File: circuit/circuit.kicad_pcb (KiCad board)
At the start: 2 copper layers, 14 parts, among them J1 POWER, J2 BLUETOOTH, J3 BUZZER, SW1 SW_PUSH_6mm, U1 ADXL359

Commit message: pcb v2.1
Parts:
- added R1: R, Resistor_SMD:R_1206_3216Metric_Pad1.30x1.75mm_HandSolder, B.Cu at (126.4, 38.3)
- added SW2: SW_DPDT_x2, Connector_PinSocket_2.00mm:PinSocket_1x03_P2.00mm_Vertical, F.Cu at (134.2, 42.2)
- C1, C2, C3, C4, C5, C6, C7, C8, U1: moved to B.Cu
- J1: footprint Connector_PinSocket_1.00mm:PinSocket_1x02_P1.00mm_Vertical -> Connector_PinSocket_2.00mm:PinSocket_1x02_P2.00mm_Vertical
- J2: footprint Connector_PinSocket_1.00mm:PinSocket_1x04_P1.00mm_Vertical -> Connector_PinSocket_2.00mm:PinSocket_1x04_P2.00mm_Vertical
- J3: footprint Connector_PinSocket_1.00mm:PinSocket_1x03_P1.00mm_Vertical -> Connector_PinSocket_2.00mm:PinSocket_1x03_P2.00mm_Vertical
- SW1: value SW_PUSH_6mm -> SW_Push; footprint Button_Switch_THT:SW_PUSH_6mm -> lowprint-pcb-ee410:sw_push_5mm
- moved SW1 68.4 mm to (128.4, 30.9)
- moved J1 37.0 mm to (134.2, 38.2), turned to 180 degrees
- moved J3 29.4 mm to (112.1, 29.4), turned to -90 degrees
- moved C8 16.3 mm to (131.7, 84.3), turned to 0 degrees
- moved C7 15.9 mm to (131.7, 87.3), turned to 0 degrees
- moved C3 13.7 mm to (125.9, 87.3)
- moved C4 13.7 mm to (125.9, 90.7)
- moved C5 8.03 mm to (131.7, 80.2), turned to 180 degrees
- moved C6 5.89 mm to (131.6, 76.8), turned to 180 degrees
- moved C2 4.68 mm to (126.0, 72.8)
- moved C1 4.68 mm to (126.0, 76.1)
- moved J2 1.00 mm to (130.7, 103.4), turned to -90 degrees
- moved U1 0.46 mm to (126.0, 82.5), turned to -90 degrees
- moved A1 0.30 mm to (102.6, 65.3)
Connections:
- A1 pad 30: 9V -> Vin
- J1 pad 2: 9V -> Net-(J1-Pin_2)
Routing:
- net Net-(A1-D13): track 4.71 -> 84.2 mm, vias 0 -> 2
- net Vin: track 0.00 -> 42.7 mm
- net BUZZER: track 27.9 -> 48.3 mm
- net 5V: track 66.0 -> 85.9 mm, vias 0 -> 2
- net 9V: track 17.8 -> 0.00 mm
- net Net-(U1-V1P8DIG): track 19.1 -> 6.15 mm
- net BT_RX: track 38.1 -> 25.3 mm, vias 1 -> 0
- net Net-(J1-Pin_2): track 0.00 -> 12.3 mm
- net Net-(A1-A4): track 5.85 -> 15.2 mm, vias 0 -> 2
- net BT_TX: track 35.2 -> 28.3 mm
- net GND: track 23.8 -> 20.1 mm, vias 1 -> 0
- net 3.3V: track 34.8 -> 37.0 mm
- net Net-(U1-V1P8ANA): track 8.96 -> 6.78 mm
- net Net-(A1-A5): track 6.28 -> 6.96 mm

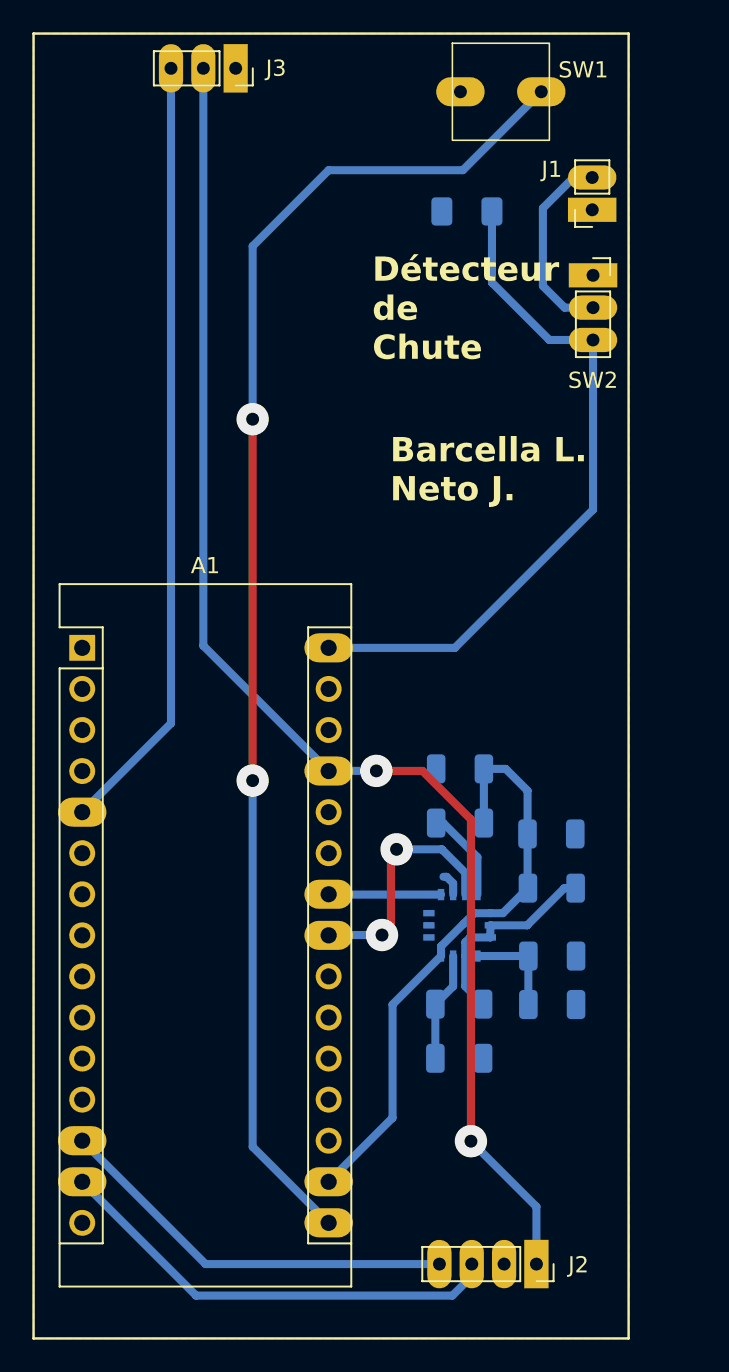
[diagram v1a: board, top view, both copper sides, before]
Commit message: Work PCB
Small Fix on PCB
+ Solve error on the resistance for the button (pcb)
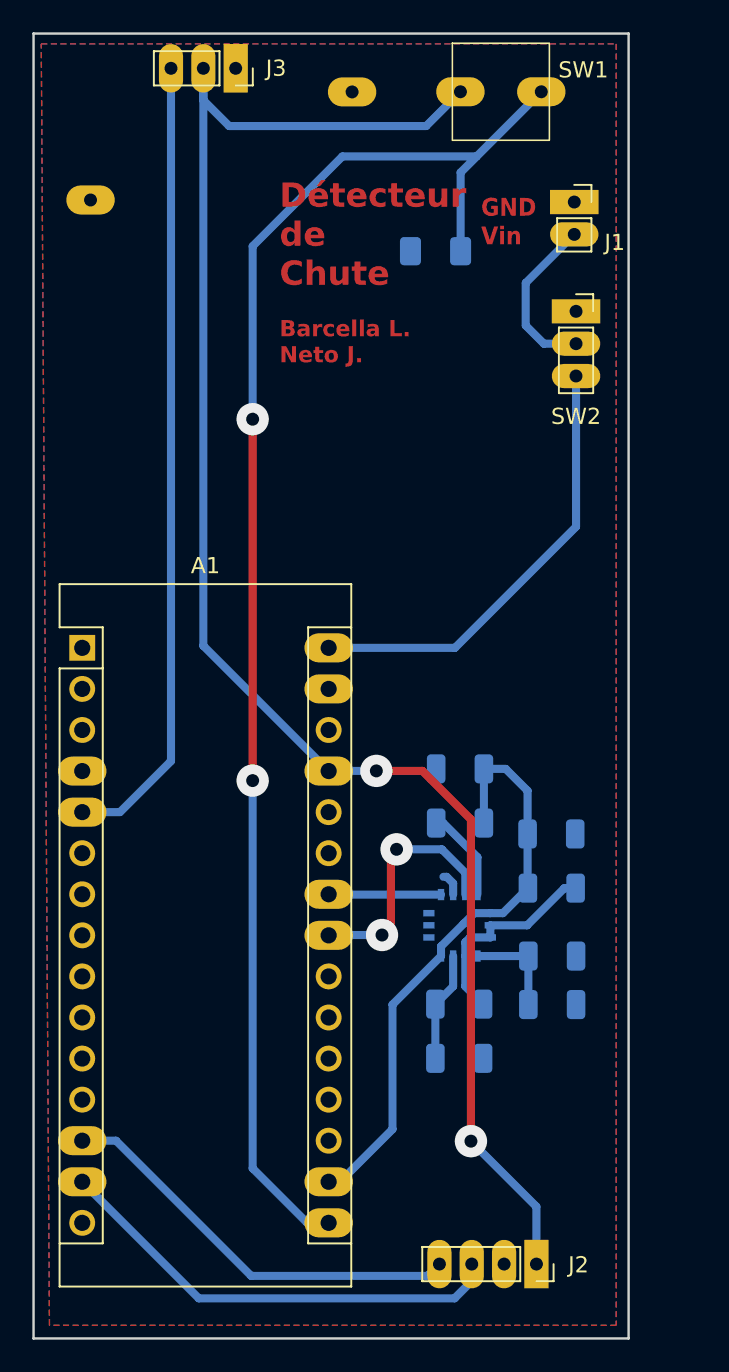
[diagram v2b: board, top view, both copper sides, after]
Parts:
- added ?: , , F.Cu at (103.1, 37.6)
- added ?: , , F.Cu at (119.3, 30.9)
- moved R1 3.13 mm to (124.5, 40.8)
- moved SW2 2.46 mm to (133.2, 44.5)
- moved J1 1.21 mm to (133.0, 37.7), turned to 0 degrees
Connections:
- R1 pad 1: Vin -> Net-(A1-D13)
- SW1 pad 1: GND -> 5V
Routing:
- net 5V: track 85.9 -> 105.3 mm
- net Vin: track 42.7 -> 27.9 mm
- net Net-(A1-D13): track 84.2 -> 95.6 mm
- net Net-(J1-Pin_2): track 12.3 -> 10.5 mm
- net BUZZER: track 48.3 -> 49.6 mm
- net BT_RX: track 25.3 -> 25.9 mm
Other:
- board outline added: 36.8 x 80.7 mm
- board text added: "GND Vin"
